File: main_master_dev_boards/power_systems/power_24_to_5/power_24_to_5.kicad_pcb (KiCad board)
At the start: 2 copper layers, 59 x 30 mm, 36 parts, among them J1 Switch_in, J10 5_in, J2 24_in, J3 GND_in, J4 PGoodMain_out, J5 ref_out, J6 5_out, J7 GND_out, J8 3v3_out, J9 PGoodBackup_out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

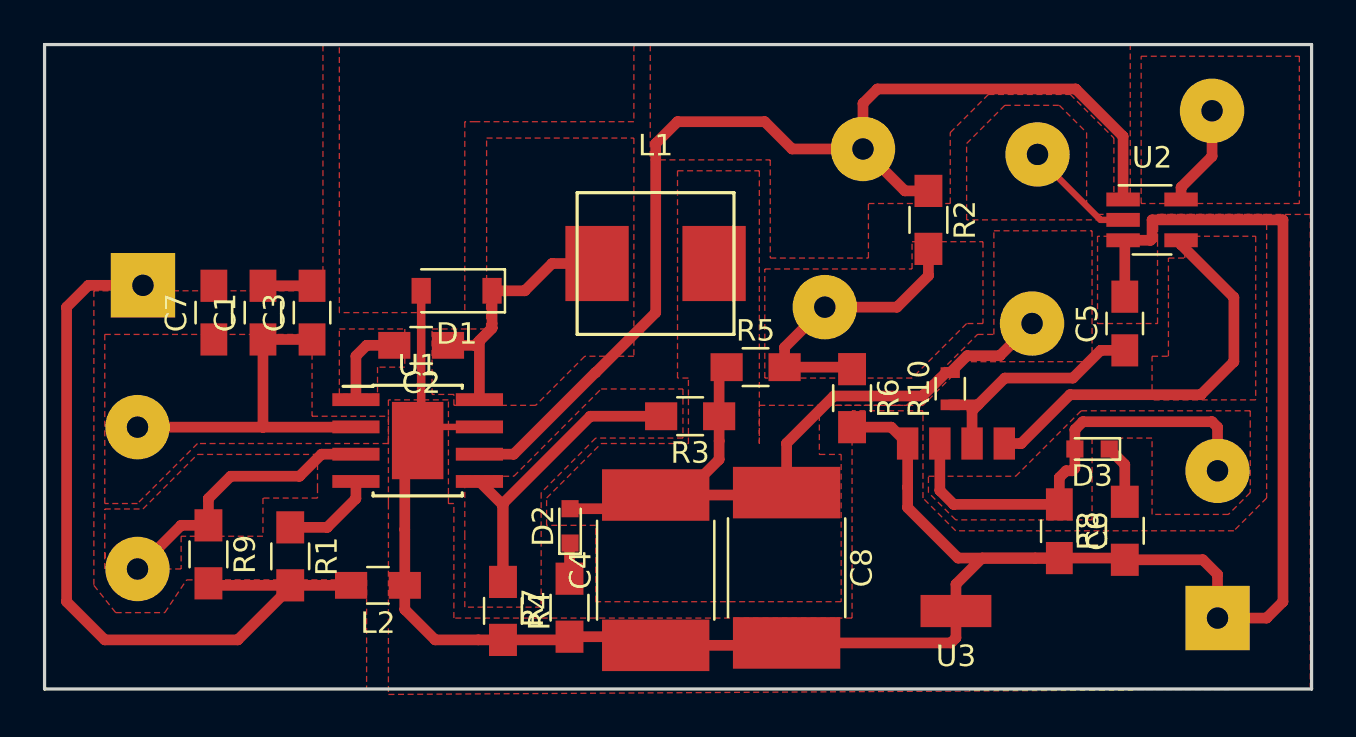
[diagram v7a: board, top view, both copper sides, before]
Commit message: Small changes to 24_to_5 converter
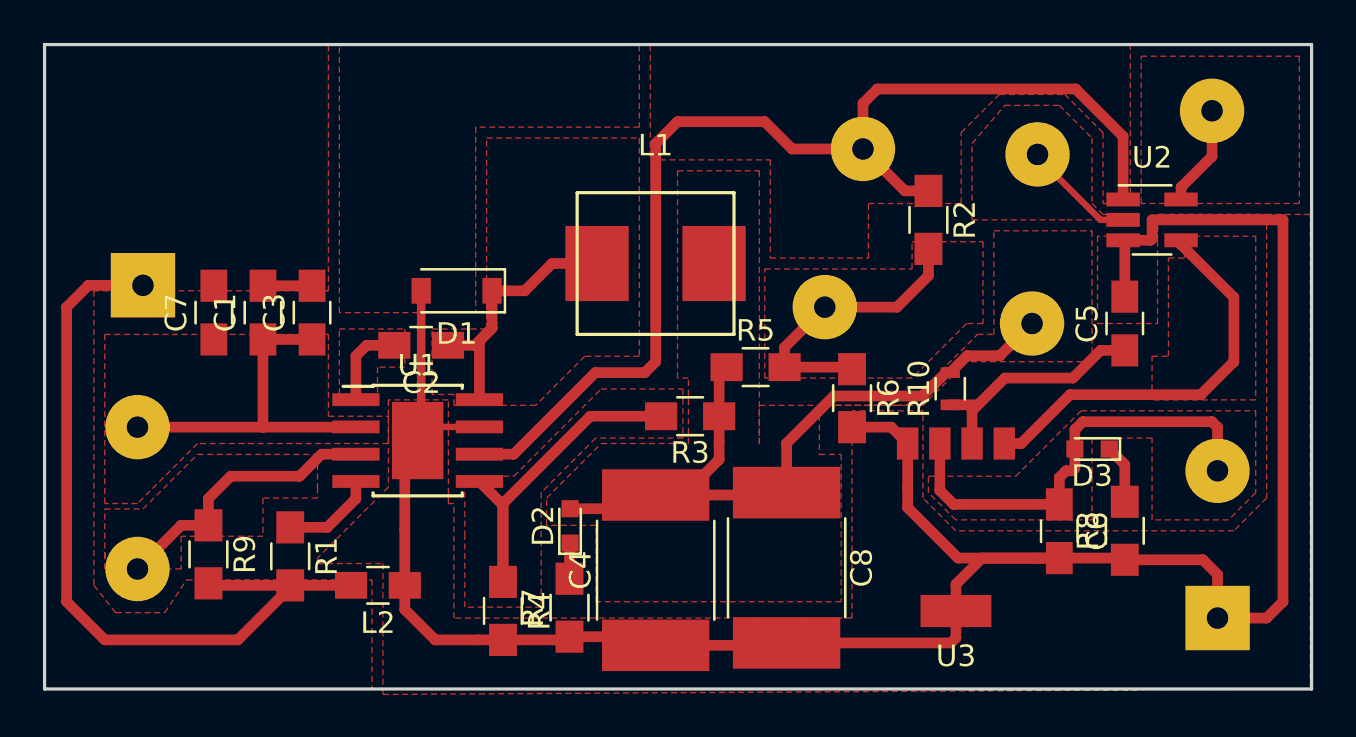
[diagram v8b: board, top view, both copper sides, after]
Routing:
- net /PG_v5_main: track 51.6 -> 53.0 mm
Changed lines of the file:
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@@
     (links 60)
     (no_connects 0)
-    (area 79.924999 33.924999 139.075001 64.083001)
+    (area 79.924999 33.43675 141.340953 64.55645)
     (thickness 1.6)
     (drawings 4)
@@
   (segment (start 93.162 56.482) (end 94.499 55.145) (width 0.5) (layer F.Cu) (net 7))
   (segment (start 94.499 55.145) (end 94.499 54.345) (width 0.5) (layer F.Cu) (net 7))
-  (segment (start 108.458 46.482) (end 108.458 38.608) (width 0.5) (layer F.Cu) (net 8))
-  (segment (start 105.648 49.276) (end 105.664 49.276) (width 0.5) (layer F.Cu) (net 8))
-  (segment (start 105.664 49.276) (end 108.458 46.482) (width 0.5) (layer F.Cu) (net 8))
+  (segment (start 100.249 53.075) (end 101.849 53.075) (width 0.5) (layer F.Cu) (net 8))
+  (segment (start 108.458 38.608) (end 109.474 37.592) (width 0.5) (layer F.Cu) (net 8))
+  (segment (start 101.849 53.075) (end 105.648 49.276) (width 0.5) (layer F.Cu) (net 8))
+  (segment (start 105.648 49.276) (end 107.95 49.276) (width 0.5) (layer F.Cu) (net 8))
+  (segment (start 107.95 49.276) (end 108.458 48.768) (width 0.5) (layer F.Cu) (net 8))
+  (segment (start 108.458 48.768) (end 108.458 38.608) (width 0.5) (layer F.Cu) (net 8))
+  (segment (start 109.474 37.592) (end 113.538 37.592) (width 0.5) (layer F.Cu) (net 8))
+  (segment (start 113.538 37.592) (end 114.808 38.862) (width 0.5) (layer F.Cu) (net 8))
+  (segment (start 114.808 38.862) (end 118.11 38.862) (width 0.5) (layer F.Cu) (net 8))
   (segment (start 121.158 40.814) (end 120.062 40.814) (width 0.5) (layer F.Cu) (net 8))
   (segment (start 120.062 40.814) (end 118.11 38.862) (width 0.5) (layer F.Cu) (net 8))
@@
   (segment (start 118.78268 36.068) (end 128.016 36.068) (width 0.5) (layer F.Cu) (net 8))
   (segment (start 128.016 36.068) (end 130.222 38.274) (width 0.5) (layer F.Cu) (net 8))
-  (segment (start 100.249 53.075) (end 101.849 53.075) (width 0.5) (layer F.Cu) (net 8))
-  (segment (start 101.849 53.075) (end 105.648 49.276) (width 0.5) (layer F.Cu) (net 8))
-  (segment (start 108.458 38.608) (end 109.474 37.592) (width 0.5) (layer F.Cu) (net 8))
-  (segment (start 109.474 37.592) (end 113.538 37.592) (width 0.5) (layer F.Cu) (net 8))
-  (segment (start 113.538 37.592) (end 114.808 38.862) (width 0.5) (layer F.Cu) (net 8))
-  (segment (start 114.808 38.862) (end 118.11 38.862) (width 0.5) (layer F.Cu) (net 8))
   (segment (start 114.46 49.022) (end 117.508 49.022) (width 0.5) (layer F.Cu) (net 9))
   (segment (start 117.508 49.022) (end 117.602 49.116) (width 0.5) (layer F.Cu) (net 9))
@@
     (polygon
       (pts
-        (xy 96.012 55.372) (xy 96.012 64.262) (xy 138.938 64.008) (xy 138.938 41.91) (xy 131.826 41.91)
+        (xy 95.758 58.166) (xy 95.758 64.262) (xy 138.938 64.008) (xy 138.938 41.91) (xy 131.826 41.91)
         (xy 131.826 42.926) (xy 129.032 42.926) (xy 129.032 44.704) (xy 129.032 46.99) (xy 131.826 46.99)
         (xy 131.826 43.18) (xy 131.826 41.91) (xy 136.906 41.91) (xy 136.906 55.118) (xy 135.382 56.642)
         (xy 122.428 56.642) (xy 120.904 55.118) (xy 120.904 51.054) (xy 117.602 51.054) (xy 117.602 60.706)
         (xy 116.84 60.706) (xy 99.06 60.706) (xy 99.06 57.15) (xy 99.06 55.372) (xy 98.806 55.372)
-        (xy 98.806 50.546) (xy 96.012 50.546) (xy 96.012 55.118)
+        (xy 98.806 50.546) (xy 96.012 50.546) (xy 96.012 54.61) (xy 92.71 57.912) (xy 92.71 58.166)
       )
     )
@@
     (polygon
       (pts
-        (xy 94.996 64.008) (xy 80.01 64.008) (xy 80.01 34.036) (xy 92.964 34.036) (xy 92.964 45.466)
+        (xy 95.25 64.008) (xy 80.01 64.008) (xy 80.01 34.036) (xy 93.218 34.036) (xy 93.218 45.466)
         (xy 86.106 45.466) (xy 82.296 45.466) (xy 82.296 59.182) (xy 83.312 60.452) (xy 85.598 60.452)
-        (xy 86.614 58.928) (xy 94.996 58.928)
+        (xy 86.614 58.928) (xy 95.25 58.928)
       )
     )
@@
     (polygon
       (pts
-        (xy 82.804 55.372) (xy 82.804 47.498) (xy 92.456 47.498) (xy 92.456 51.308) (xy 96.012 51.308)
+        (xy 82.804 55.372) (xy 82.804 47.498) (xy 93.218 47.498) (xy 93.218 51.308) (xy 96.012 51.308)
         (xy 96.012 52.324) (xy 96.012 52.578) (xy 87.122 52.578) (xy 84.328 55.372)
       )
@@
     (polygon
       (pts
-        (xy 98.044 50.292) (xy 98.044 47.244) (xy 100.584 47.244) (xy 100.584 38.354) (xy 107.442 38.354)
-        (xy 107.442 48.514) (xy 105.156 48.514) (xy 102.87 50.8) (xy 99.06 50.8) (xy 99.06 50.292)
+        (xy 98.044 50.292) (xy 98.044 47.244) (xy 100.584 47.244) (xy 100.584 38.354) (xy 107.696 38.354)
+        (xy 107.696 48.514) (xy 105.156 48.514) (xy 102.87 50.8) (xy 99.06 50.8) (xy 99.06 50.292)
       )
     )
@@
     (polygon
       (pts
-        (xy 136.144 51.562) (xy 136.144 54.864) (xy 135.128 55.88) (xy 131.572 55.88) (xy 131.572 52.324)
+        (xy 136.398 51.562) (xy 136.398 54.864) (xy 135.128 56.134) (xy 131.572 56.134) (xy 131.572 52.324)
         (xy 128.778 52.324) (xy 128.778 56.134) (xy 122.428 56.134) (xy 121.158 54.864) (xy 121.158 54.102)
-        (xy 125.222 54.102) (xy 128.27 51.054) (xy 136.144 51.054)
+        (xy 125.222 54.102) (xy 128.27 51.054) (xy 136.398 51.054)
       )
     )
@@
       (pts
         (xy 108.204 39.37) (xy 113.792 39.37) (xy 113.792 43.942) (xy 118.364 43.942) (xy 118.364 41.402)
-        (xy 122.174 41.402) (xy 122.174 38.1) (xy 123.952 36.322) (xy 127.762 36.322) (xy 129.794 38.354)
-        (xy 129.794 41.402) (xy 130.556 41.402) (xy 130.556 34.036) (xy 108.204 34.036)
+        (xy 122.682 41.402) (xy 122.682 38.1) (xy 124.46 36.322) (xy 127.508 36.322) (xy 129.286 38.1)
+        (xy 129.286 41.402) (xy 130.556 41.402) (xy 130.556 34.036) (xy 108.204 34.036)
       )
     )
@@
     (polygon
       (pts
-        (xy 93.726 46.482) (xy 93.726 34.036) (xy 107.442 34.036) (xy 107.442 37.592) (xy 100.076 37.592)
-        (xy 99.568 37.592) (xy 99.568 46.482)
+        (xy 93.726 46.482) (xy 93.726 34.036) (xy 107.696 34.036) (xy 107.696 37.846) (xy 100.076 37.846)
+        (xy 100.076 46.482)
       )
     )
@@
     (polygon
       (pts
-        (xy 130.556 42.164) (xy 127.508 42.164) (xy 122.936 42.164) (xy 122.936 38.608) (xy 124.714 36.83)
-        (xy 127.254 36.83) (xy 128.524 38.1) (xy 128.524 41.402) (xy 129.032 41.91) (xy 130.556 41.91)
+        (xy 130.556 42.164) (xy 127.508 42.164) (xy 123.19 42.164) (xy 123.19 38.608) (xy 124.714 36.83)
+        (xy 127.254 36.83) (xy 128.778 38.354) (xy 128.778 41.402) (xy 129.286 41.91) (xy 130.556 41.91)
       )
     )
